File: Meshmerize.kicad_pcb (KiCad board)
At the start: 2 copper layers, 113.9 x 108.8 mm, 62 parts, among them J1 Conn_01x19_Male, J2 Conn_01x19_Male, J3 Conn_01x04_Female, M1 Motor_DC, M2 Motor_DC, U1 LM324, U2 ESP32-DEVKITC-32D, U3 TCRT5000, U4 TCRT5000, U5 MT3608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

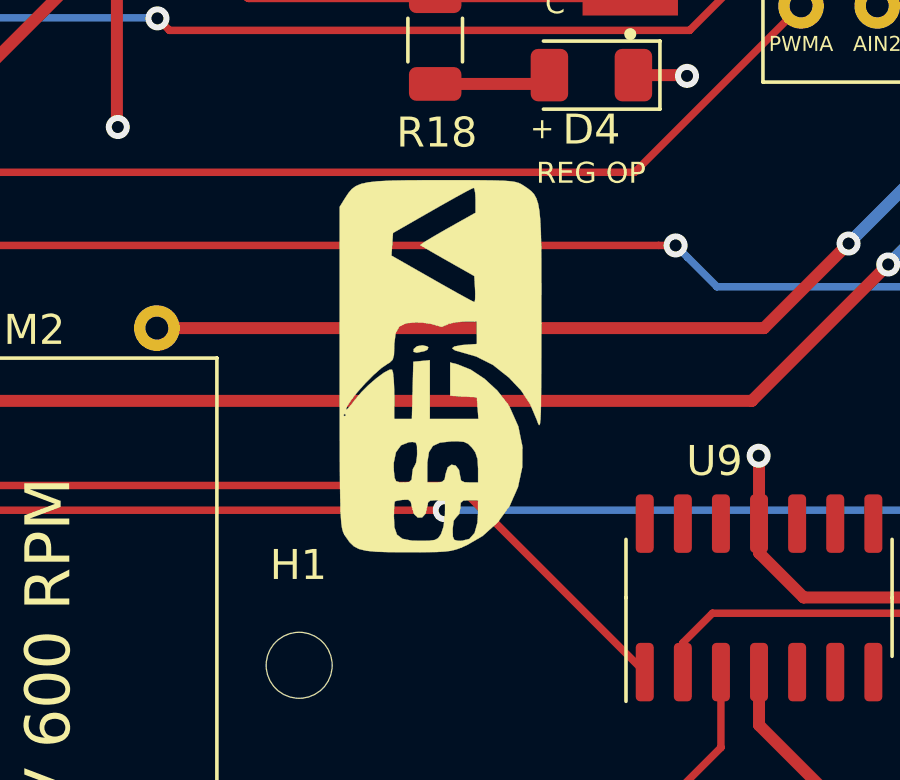
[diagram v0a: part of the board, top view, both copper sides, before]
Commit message: Shortened MAZEBLAZE title on B.silk
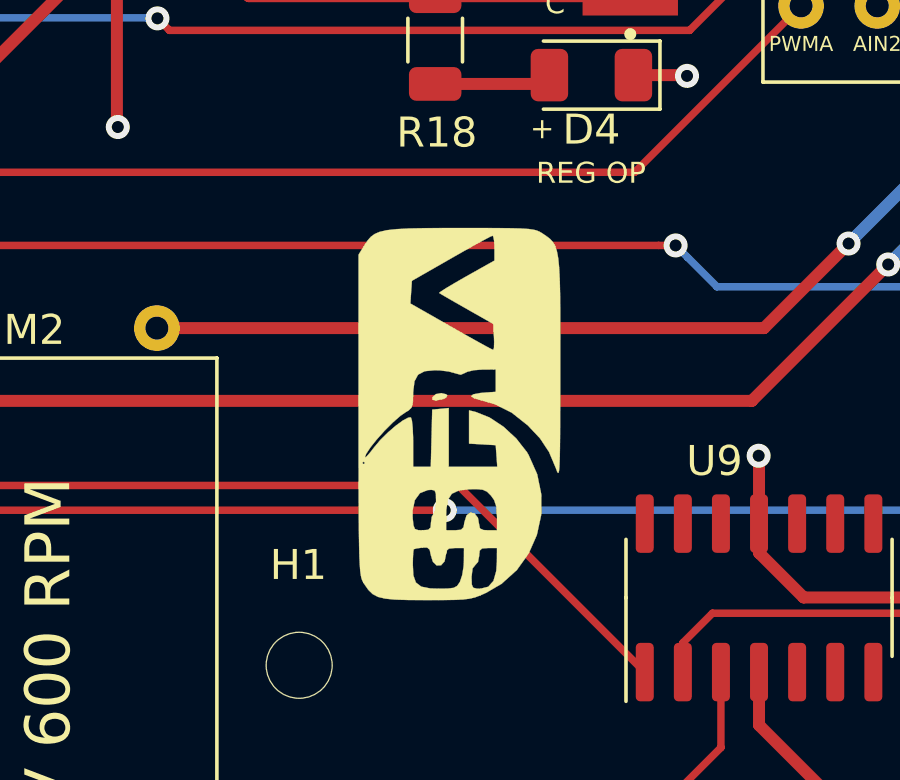
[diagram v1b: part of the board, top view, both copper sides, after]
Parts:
- moved G*** 1.71 mm to (165.1, 112.7)
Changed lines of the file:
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@@
-(kicad_pcb (version 20171130) (host pcbnew 5.1.10-88a1d61d58~90~ubuntu20.04.1)
+(kicad_pcb (version 20171130) (host pcbnew 5.1.5+dfsg1-2build2)
   (general
     (thickness 1.6)
@@
   )
   (module SRA_Logo:sralogo (layer F.Cu)
-    (at 164.43452 111.125 90)
+    (at 165.06444 112.72012 90)
     (fp_text reference G*** (at 0 0 270) (layer F.SilkS) hide
       (effects (font (size 1.524 1.524) (thickness 0.3)))
@@
     (effects (font (size 1.6 1.6) (thickness 0.3)) (justify mirror))
   )
-  (gr_text MAZEBLAZE (at 147.63496 92.05976 -90) (layer B.SilkS)
-    (effects (font (size 5 5) (thickness 1)) (justify mirror))
+  (gr_text MAZEBLAZE (at 147.55368 91.40952 -90) (layer B.SilkS)
+    (effects (font (size 4 4) (thickness 1)) (justify mirror))
   )
   (gr_text "N20 6V 600 RPM" (at 150.7871 59.055 270) (layer F.SilkS)
